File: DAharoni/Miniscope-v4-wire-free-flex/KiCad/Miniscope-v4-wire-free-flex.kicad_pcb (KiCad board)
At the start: 2 copper layers, 12 x 15.8 mm, 3 parts, among them J1 Conn_01x20, J2 Conn_01x14, J3 Conn_01x20

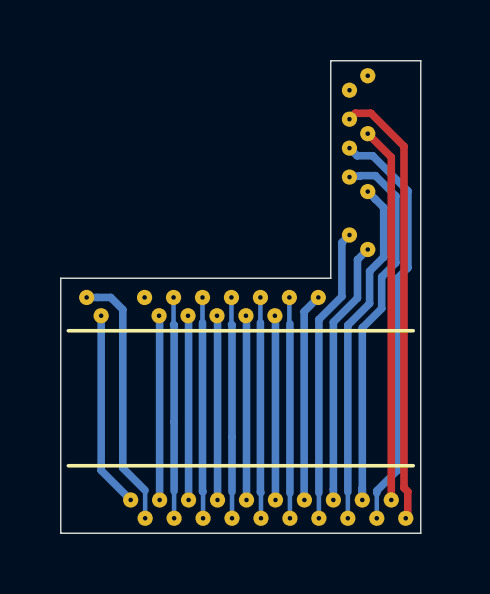
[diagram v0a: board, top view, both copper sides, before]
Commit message: Finish wire-free MCU PCB and flexPC for first fab run (version 0.1)
The committed gerbers were submitted to JLCPCB and PCBway on 09/21/2019
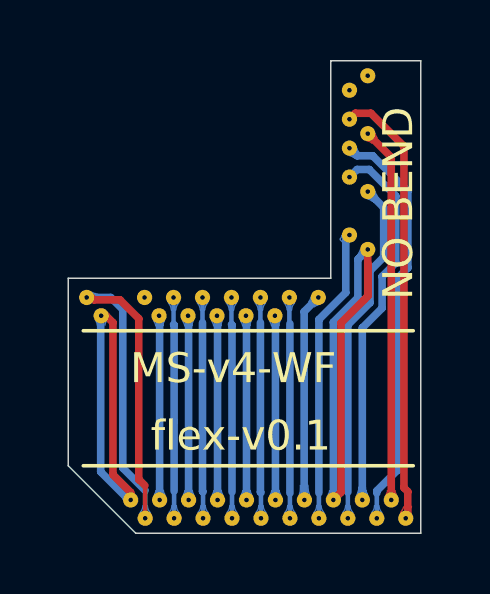
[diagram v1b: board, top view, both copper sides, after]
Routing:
- net +1V8: track 8.82 -> 18.7 mm
- net GND: track 8.64 -> 17.4 mm
- net +3V3: track 6.55 -> 13.2 mm
- added copper zone on B.Cu, net /DOUT6
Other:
- board size 12 x 15.8 mm -> 11.8 x 15.8 mm
- board text added: "MS-v4-WF"
- board text added: "NO BEND"
- board text added: "flex-v0.1"
